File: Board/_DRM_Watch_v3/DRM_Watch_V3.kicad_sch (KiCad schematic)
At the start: 93 parts, among them J1 TYPE-C-31-M-12, J2 687110149022, Q1 2N7002LT1G, U1 ESP32-S2, U3 TP4056, U4 DS3231S, Y1 XRCGB48M000F0Z00R0

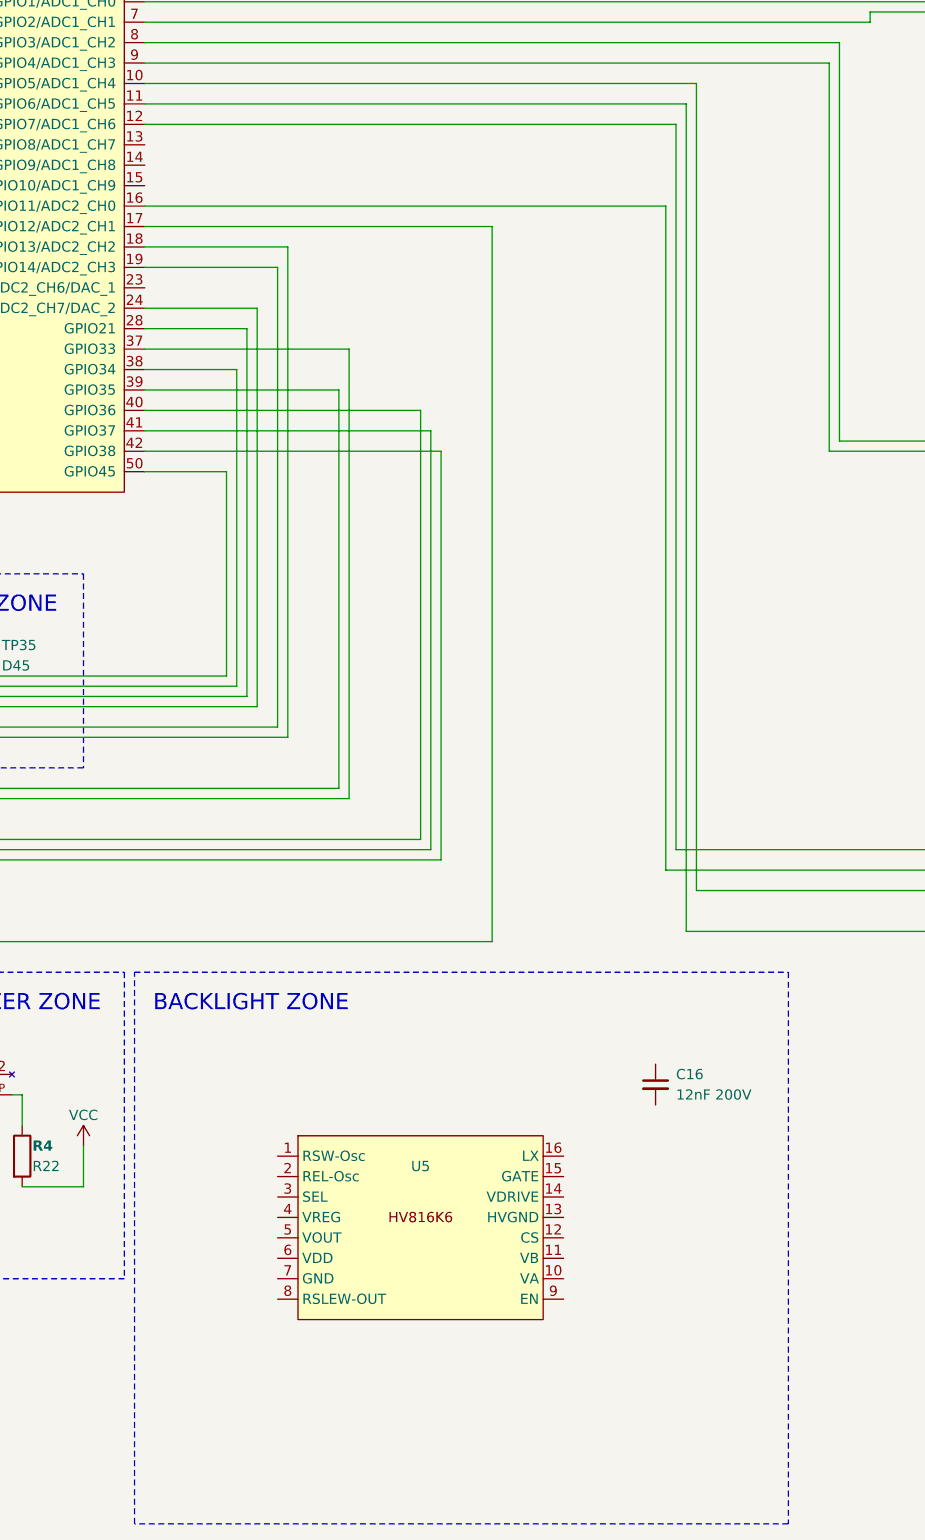
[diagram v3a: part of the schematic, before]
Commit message: 2024-02-25 Board: Added symbols for HV857 2024-02-26 Board: Added case outline to board project 2024-02-26 Schematic: Added elements for EL Backlight
2024-02-25 Board: Added symbols for HV857
2024-02-26 Board: Added case outline to board project
2024-02-26 Schematic: Added elements for EL Backlight
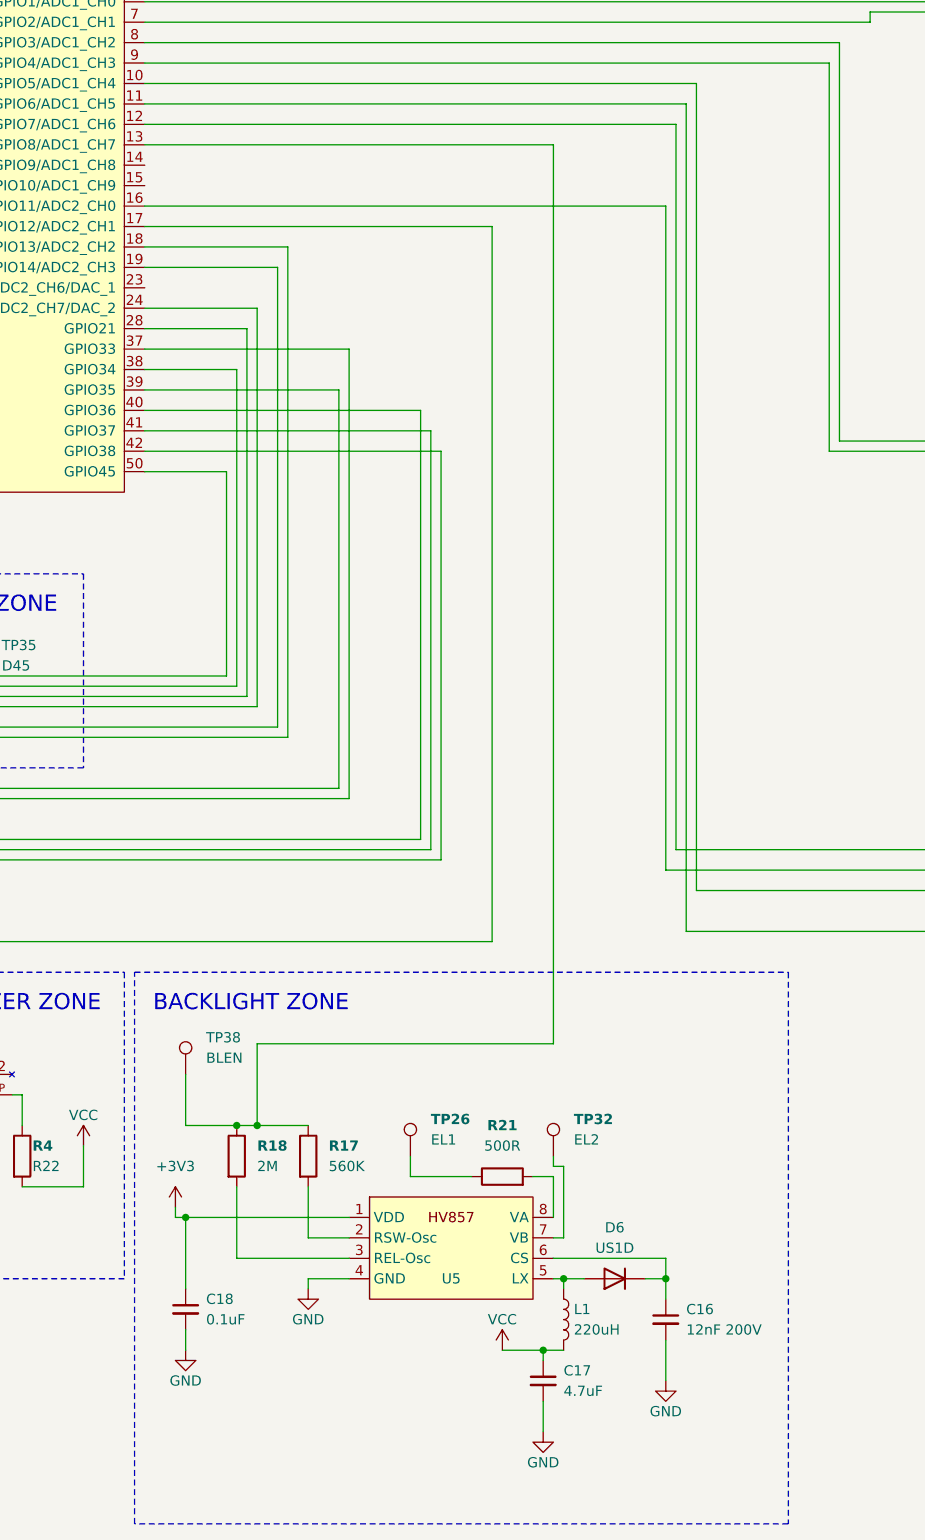
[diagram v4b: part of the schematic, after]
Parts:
- removed U5: ~, Package_DFN_QFN:QFN-16-1EP_4x4mm_P0.65mm_EP2.5x2.5mm, symbol Project-Lib:HV816K6
- added C17: 4.7uF, Project-Lib:C_1206, symbol Device:C_Small
- added C18: 0.1uF, Project-Lib:C_1206, symbol Device:C_Small
- added D6: US1D, Diode_SMD:D_SMA, symbol Diode:US1D
- added L1: 220uH, Project-Lib:Inductor-L_1210_3225Metric, symbol Device:L
- added R17: 560K, Project-Lib:R_0603_1608Metric, symbol Device:R
- added R18: 2M, Project-Lib:R_0603_1608Metric, symbol Device:R
- added R21: 500R, Project-Lib:R_0603_1608Metric, symbol Device:R
- added TP26: EL1, Project-Lib:TestPoint_Pad, symbol Project-Lib:TestPoint
- added TP32: EL2, Project-Lib:TestPoint_Pad, symbol Project-Lib:TestPoint
- added TP38: BLEN, Project-Lib:TestPoint_Pad, symbol Project-Lib:TestPoint
- added U5: ~, Project-Lib:HV857, symbol Project-Lib:HV857
- C16: footprint Capacitor_SMD:C_1206_3216Metric -> Project-Lib:C_1206
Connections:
- net +3V3: now also C18.1, U5.1 (VDD)
- net GND: now also C16.2, C17.2, C18.2, U5.4 (GND)
- net VCC: now also C17.1, L1.2
- net at U1.13 (GPIO8/ADC1_CH7): now also R17.1, R18.1, TP38.1
- net at C16.1: now also D6.1 (K), U5.6 (CS)
- new net: R21.1, TP26.1
- new net: R21.2, U5.8 (VA)
- new net: R18.2, U5.3 (REL-Osc)
- new net: R17.2, U5.2 (RSW-Osc)
- new net: D6.2 (A), L1.1, U5.5 (LX)
- new net: TP32.1, U5.7 (VB)
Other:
- moved on the sheet: C16

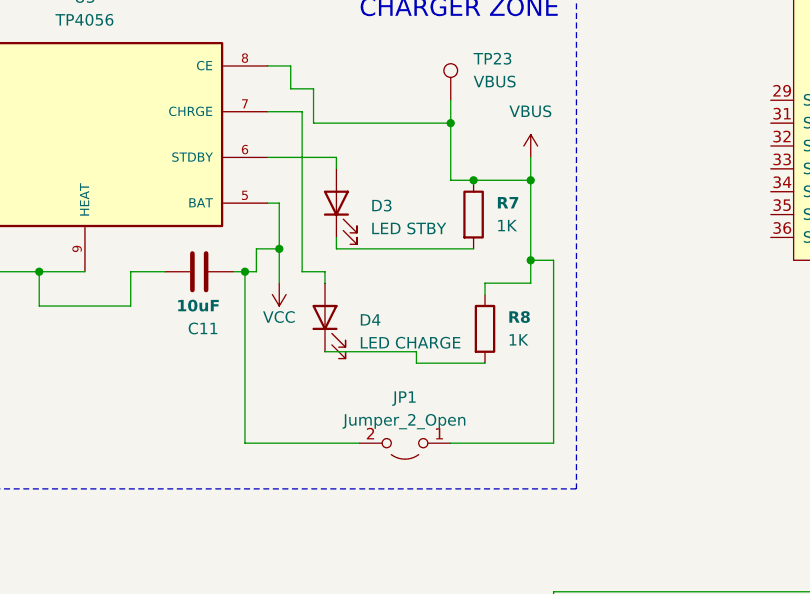
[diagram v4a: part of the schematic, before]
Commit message: 2024-02-27 Board: Destroyed all the board wiring and start over.
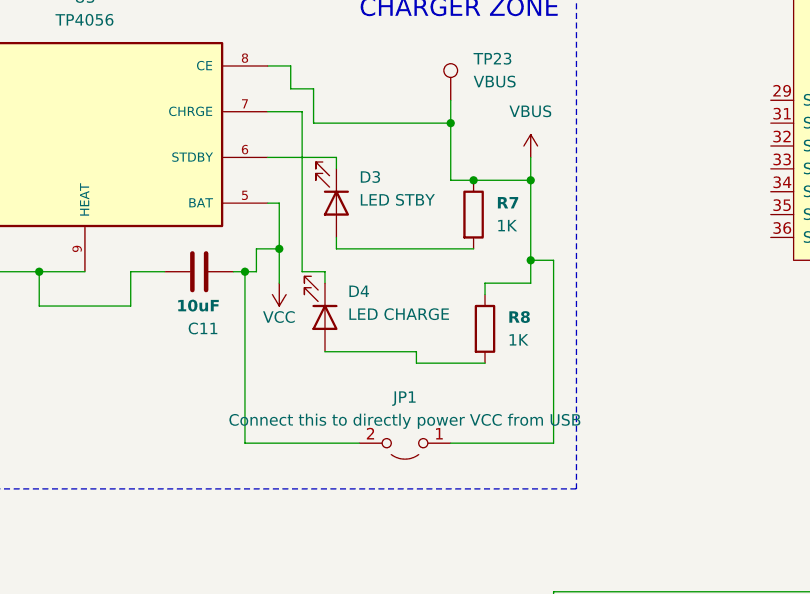
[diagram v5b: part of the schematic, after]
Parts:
- JP1: value Jumper_2_Open -> Connect this to directly power VCC from USB
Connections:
- net at U3.6 (STDBY): now also D3.1 (K); no longer D3.2 (A)
- net at U3.7 (CHRGE): now also D4.1 (K); no longer D4.2 (A)
- net at R8.2: now also D4.2 (A); no longer D4.1 (K)
- net at R7.2: now also D3.2 (A); no longer D3.1 (K)
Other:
- moved on the sheet: D3, D4
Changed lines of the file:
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@@
       (effects (font (size 1.27 1.27)))
     )
-    (property "Value" "Jumper_2_Open" (at 100.33 168.91 0)
+    (property "Value" "Connect this to directly power VCC from USB" (at 100.33 168.91 0)
       (effects (font (size 1.27 1.27)))
     )
@@
     )
   )
-  (symbol (lib_id "Device:LED") (at 91.44 157.48 90) (unit 1)
+  (symbol (lib_id "Device:LED") (at 91.44 157.48 270) (unit 1)
     (in_bom no) (on_board yes) (dnp no) (fields_autoplaced)
-    (property "Reference" "D4" (at 95.25 157.7975 90)
-      (effects (font (size 1.27 1.27)) (justify right))
+    (property "Reference" "D4" (at 93.98 154.6225 90)
+      (effects (font (size 1.27 1.27)) (justify left))
     )
-    (property "Value" "LED CHARGE" (at 95.25 160.3375 90)
-      (effects (font (size 1.27 1.27)) (justify right))
+    (property "Value" "LED CHARGE" (at 93.98 157.1625 90)
+      (effects (font (size 1.27 1.27)) (justify left))
     )
     (property "Footprint" "Project-Lib:HOLE_LED_0805_2012Metric" (at 91.44 157.48 0)
@@
     )
   )
-  (symbol (lib_id "Device:LED") (at 92.71 144.78 90) (unit 1)
+  (symbol (lib_id "Device:LED") (at 92.71 144.78 270) (unit 1)
     (in_bom no) (on_board yes) (dnp no) (fields_autoplaced)
-    (property "Reference" "D3" (at 96.52 145.0975 90)
-      (effects (font (size 1.27 1.27)) (justify right))
+    (property "Reference" "D3" (at 95.25 141.9225 90)
+      (effects (font (size 1.27 1.27)) (justify left))
     )
-    (property "Value" "LED STBY" (at 96.52 147.6375 90)
-      (effects (font (size 1.27 1.27)) (justify right))
+    (property "Value" "LED STBY" (at 95.25 144.4625 90)
+      (effects (font (size 1.27 1.27)) (justify left))
     )
     (property "Footprint" "Project-Lib:HOLE_LED_0805_2012Metric" (at 92.71 144.78 0)

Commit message: 2024-02-27 Board: Moved elements and more wiring
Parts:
- D6: footprint Diode_SMD:D_SMA -> Project-Lib:US1D
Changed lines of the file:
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@@
       (effects (font (size 1.27 1.27)))
     )
-    (property "Footprint" "Diode_SMD:D_SMA" (at 275.59 244.475 0)
+    (property "Footprint" "Project-Lib:US1D" (at 275.59 244.475 0)
       (effects (font (size 1.27 1.27)) hide)
     )

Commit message: 2024-04-01 v2.03 Виправлено баг: Дисплей постійно мигав при оновленнях 2024-04-01 Доповнено документацію
2024-04-01 v2.03 Виправлено баг: Дисплей постійно мигав при оновленнях
2024-04-01 Доповнено документацію
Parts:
- C2, C3: now in the parts list
- LS1: Link (none) -> https://www.aliexpress.us/item/1005003620083880.html; Link2 (none) -> https://eu.mouser.com/ProductDetail/CUI-Devices/CMT-7525S-S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; now in the parts list
- U1: value ESP32-S2 -> Espressif ESP32-S2, QFN56; Link (none) -> https://www.tme.eu/en/details/esp32s2/iot-wifi-bluetooth-mo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; now in the parts list
- Y1: value XRCGB48M000F0Z00R0 -> 3225 4PIN 40Mhz 3.2*2.5mm Passive SMD Quartz Resonator Crystal; Availability In Stock -> (none); Check_prices https://www.snapeda.com/parts/XRCGB48M000F0Z00R0/Murata/vie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 -> (none); Link (none) -> https://www.aliexpress.us/item/1005004689346275.html; MANUFACTURER Murata Electronics -> (none); MAXIMUM_PACKAGE_HEIGHT 0.7 mm -> (none); MF Murata -> (none); MP XRCGB48M000F0Z00R0 -> (none); PARTREV N/A -> (none); Package SMD-4 Murata -> 3225 smd; Price None -> (none); Purchase-URL https://www.snapeda.com/api/url_track_click_mouser/?unipart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 -> (none); STANDARD Manufacturer Recommendations -> (none); SnapEDA_Link https://www.snapeda.com/parts/XRCGB48M000F0Z00R0/Murata/vie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 -> (none); now in the parts list
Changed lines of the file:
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@@
   )
   (symbol (lib_id "Project-Lib:ESP32-S2") (at 179.07 110.49 0) (unit 1)
-    (in_bom no) (on_board yes) (dnp no) (fields_autoplaced)
+    (in_bom yes) (on_board yes) (dnp no) (fields_autoplaced)
     (property "Reference" "U1" (at 181.2641 153.67 0)
       (effects (font (size 1.27 1.27)) (justify left))
     )
-    (property "Value" "ESP32-S2" (at 181.2641 156.21 0)
+    (property "Value" "Espressif ESP32-S2, QFN56" (at 181.2641 156.21 0)
       (effects (font (size 1.27 1.27)) (justify left))
     )
@@
     )
     (property "Datasheet" "https://www.espressif.com/sites/default/files/documentation/esp32-s2_datasheet_en.pdf" (at 179.07 167.64 0)
+      (effects (font (size 1.27 1.27)) hide)
+    )
+    (property "Link" "https://www.tme.eu/en/details/esp32s2/iot-wifi-bluetooth-modules/espressif/esp32-s2/" (at 179.07 110.49 0)
       (effects (font (size 1.27 1.27)) hide)
     )
@@
   )
   (symbol (lib_id "Device:C") (at 73.66 101.6 0) (unit 1)
-    (in_bom no) (on_board yes) (dnp no) (fields_autoplaced)
+    (in_bom yes) (on_board yes) (dnp no) (fields_autoplaced)
     (property "Reference" "C2" (at 77.47 100.33 0)
       (effects (font (size 1.27 1.27)) (justify left))
@@
   )
   (symbol (lib_id "Device:C") (at 73.66 82.55 0) (unit 1)
-    (in_bom no) (on_board yes) (dnp no) (fields_autoplaced)
+    (in_bom yes) (on_board yes) (dnp no) (fields_autoplaced)
     (property "Reference" "C3" (at 77.47 81.28 0)
       (effects (font (size 1.27 1.27)) (justify left))
@@
   )
   (symbol (lib_id "Project-Lib:XRCGB48M000F0Z00R0") (at 87.63 93.98 270) (mirror x) (unit 1)
-    (in_bom no) (on_board yes) (dnp no)
+    (in_bom yes) (on_board yes) (dnp no)
     (property "Reference" "Y1" (at 81.28 88.9 90)
       (effects (font (size 1.27 1.27)) (justify left))
     )
-    (property "Value" "XRCGB48M000F0Z00R0" (at 74.93 91.44 90)
+    (property "Value" "3225 4PIN 40Mhz 3.2*2.5mm Passive SMD Quartz Resonator Crystal" (at 74.93 91.44 90)
       (effects (font (face "KiCad Font") (size 0.5 0.5)) (justify left))
     )
@@
       (effects (font (size 1.27 1.27)) hide)
     )
-    (property "MF" "Murata" (at 87.63 93.98 0)
-      (effects (font (size 1.27 1.27)) (justify bottom) hide)
-    )
-    (property "MAXIMUM_PACKAGE_HEIGHT" "0.7 mm" (at 87.63 93.98 0)
-      (effects (font (size 1.27 1.27)) (justify bottom) hide)
-    )
-    (property "Package" "SMD-4 Murata" (at 87.63 93.98 0)
-      (effects (font (size 1.27 1.27)) (justify bottom) hide)
-    )
-    (property "Price" "None" (at 87.63 93.98 0)
-      (effects (font (size 1.27 1.27)) (justify bottom) hide)
-    )
-    (property "Check_prices" "https://www.snapeda.com/parts/XRCGB48M000F0Z00R0/Murata/view-part/?ref=eda" (at 87.63 93.98 0)
-      (effects (font (size 1.27 1.27)) (justify bottom) hide)
-    )
-    (property "STANDARD" "Manufacturer Recommendations" (at 87.63 93.98 0)
-      (effects (font (size 1.27 1.27)) (justify bottom) hide)
-    )
-    (property "PARTREV" "N/A" (at 87.63 93.98 0)
-      (effects (font (size 1.27 1.27)) (justify bottom) hide)
-    )
-    (property "SnapEDA_Link" "https://www.snapeda.com/parts/XRCGB48M000F0Z00R0/Murata/view-part/?ref=snap" (at 87.63 93.98 0)
-      (effects (font (size 1.27 1.27)) (justify bottom) hide)
-    )
-    (property "MP" "XRCGB48M000F0Z00R0" (at 87.63 93.98 0)
-      (effects (font (size 1.27 1.27)) (justify bottom) hide)
-    )
-    (property "Purchase-URL" "https://www.snapeda.com/api/url_track_click_mouser/?unipart_id=2497019&manufacturer=Murata&part_name=XRCGB48M000F0Z00R0&search_term=40mhz" (at 87.63 93.98 0)
-      (effects (font (size 1.27 1.27)) (justify bottom) hide)
-    )
-    (property "Description" "\nCrystals 40.000Mhz 100ppm Init Freq Tol\n" (at 87.63 93.98 0)
-      (effects (font (size 1.27 1.27)) (justify bottom) hide)
-    )
-    (property "Availability" "In Stock" (at 87.63 93.98 0)
-      (effects (font (size 1.27 1.27)) (justify bottom) hide)
-    )
-    (property "MANUFACTURER" "Murata Electronics" (at 87.63 93.98 0)
-      (effects (font (size 1.27 1.27)) (justify bottom) hide)
+    (property "Package" "3225 smd" (at 87.63 93.98 0)
+      (effects (font (size 1.27 1.27)) (justify bottom) hide)
+    )
+    (property "Link" "https://www.aliexpress.us/item/1005004689346275.html" (at 87.63 93.98 90)
+      (effects (font (size 1.27 1.27)) hide)
     )
     (pin "1")
@@
   )
   (symbol (lib_id "Project-Lib:CMT-7525S-SMT") (at 195.58 226.06 270) (unit 1)
-    (in_bom no) (on_board yes) (dnp no)
+    (in_bom yes) (on_board yes) (dnp no)
     (property "Reference" "LS1" (at 195.58 229.87 90)
       (effects (font (size 1 1)))
@@
       (effects (font (size 1.27 1.27)) (justify bottom) hide)
     )
+    (property "Link" "https://www.aliexpress.us/item/1005003620083880.html" (at 195.58 226.06 90)
+      (effects (font (size 1.27 1.27)) hide)
+    )
+    (property "Link2" "https://eu.mouser.com/ProductDetail/CUI-Devices/CMT-7525S-SMT-TR?qs=qCxwlXJ4fnw4ZHFvNib47A%3D%3D" (at 195.58 226.06 90)
+      (effects (font (size 1.27 1.27)) hide)
+    )
     (pin "N")

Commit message: doc
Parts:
- U3: Availability Not in stock -> (none); Check_prices https://www.snapeda.com/parts/TP4056/Texas+Instruments/view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 -> (none); Link (none) -> https://www.alibaba.com/product-detail/TC4056A-SOP-8-is-com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; Package None -> (none); Price None -> (none); SnapEDA_Link https://www.snapeda.com/parts/TP4056/Texas+Instruments/view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 -> (none)
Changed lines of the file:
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@@
       (effects (font (size 1.27 1.27)) (justify bottom) hide)
     )
-    (property "Datasheet" "" (at 64.77 137.16 0)
+    (property "Datasheet" "https://dlnmh9ip6v2uc.cloudfront.net/datasheets/Prototyping/TP4056.pdf" (at 64.77 137.16 0)
       (effects (font (size 1.27 1.27)) hide)
     )
@@
       (effects (font (size 1.27 1.27)) (justify bottom) hide)
     )
-    (property "Description" "\nCharger Li-Ion Article 1A protection, module with IO TP4056 (micro USB)\n" (at 64.77 109.22 0)
-      (effects (font (size 1.27 1.27)) (justify bottom) hide)
-    )
-    (property "Package" "None" (at 64.77 111.76 0)
-      (effects (font (size 1.27 1.27)) (justify bottom) hide)
-    )
-    (property "Price" "None" (at 64.77 114.3 0)
-      (effects (font (size 1.27 1.27)) (justify bottom) hide)
-    )
-    (property "SnapEDA_Link" "https://www.snapeda.com/parts/TP4056/Texas+Instruments/view-part/?ref=snap" (at 64.77 109.22 0)
-      (effects (font (size 1.27 1.27)) (justify bottom) hide)
-    )
     (property "MP" "TP4056" (at 67.31 119.38 0)
       (effects (font (size 1.27 1.27)) (justify bottom) hide)
     )
-    (property "Availability" "Not in stock" (at 64.77 109.22 0)
-      (effects (font (size 1.27 1.27)) (justify bottom) hide)
-    )
-    (property "Check_prices" "https://www.snapeda.com/parts/TP4056/Texas+Instruments/view-part/?ref=eda" (at 64.77 109.22 0)
-      (effects (font (size 1.27 1.27)) (justify bottom) hide)
+    (property "Link" "https://www.alibaba.com/product-detail/TC4056A-SOP-8-is-compatible-with_1600806443781.html" (at 64.77 137.16 0)
+      (effects (font (size 1.27 1.27)) hide)
     )
     (pin "5")
